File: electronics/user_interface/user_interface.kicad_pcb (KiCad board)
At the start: 2 copper layers, 100 x 100 mm, 44 parts, among them J1 Conn_01x06, J2 Conn_02x05_Odd_Even, U1 PCF8574, U2 PCF8574

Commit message: added ESD protection
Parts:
- added D5: 5V, SquantorDiodes:SOD-523, F.Cu at (114.0, 111.0)
- added D6: 5V, SquantorDiodes:SOD-523, F.Cu at (114.0, 131.0)
- added D7: 5V, SquantorDiodes:SOD-523, F.Cu at (158.0, 121.0)
- added D8: 5V, SquantorDiodes:SOD-523, F.Cu at (158.0, 141.0)
- moved R13 0.15 mm to (114.0, 133.0)
- moved R16 0.15 mm to (114.0, 135.0)
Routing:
- net Net-(D1-Pad2): track 10.3 -> 12.4 mm
- net /VSS: track 13.6 -> 14.4 mm, vias 0 -> 1
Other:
- rule pad_to_mask_clearance: 0.2 -> 0.1
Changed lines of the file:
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@@
     (thickness 1.6)
     (drawings 6)
-    (tracks 42)
+    (tracks 47)
     (zones 0)
-    (modules 44)
+    (modules 48)
     (nets 37)
   )
@@
     (pad_size 1.524 1.524)
     (pad_drill 0.762)
-    (pad_to_mask_clearance 0.2)
+    (pad_to_mask_clearance 0.1)
     (aux_axis_origin 0 0)
     (visible_elements FFFFFF7F)
@@
     (add_net "Net-(U2-Pad9)")
   )
+  (module SquantorDiodes:SOD-523 (layer F.Cu)
+    (at 158 141)
+    (fp_text reference D8 (at 0 -1.3) (layer F.SilkS)
+      (effects (font (size 1 1) (thickness 0.15)))
+    )
+    (fp_text value 5V (at 0 1.4) (layer F.Fab)
+      (effects (font (size 1 1) (thickness 0.15)))
+    )
+    (fp_line (start -1.1 -0.6) (end 1.1 -0.6) (layer F.CrtYd) (width 0.05))
+    (fp_line (start 1.1 -0.6) (end 1.1 0.6) (layer F.CrtYd) (width 0.05))
+    (fp_line (start 1.1 0.6) (end -1.1 0.6) (layer F.CrtYd) (width 0.05))
+    (fp_line (start -1.1 0.6) (end -1.1 -0.6) (layer F.CrtYd) (width 0.05))
+    (fp_line (start -0.3 -0.4) (end 0.3 -0.4) (layer F.SilkS) (width 0.15))
+    (fp_line (start 0.3 0.4) (end -0.3 0.4) (layer F.SilkS) (width 0.15))
+    (fp_line (start -0.3 -0.4) (end -0.3 0.4) (layer F.SilkS) (width 0.15))
+    (pad 2 smd rect (at 0.7 0) (size 0.5 0.6) (layers F.Cu F.Paste F.Mask)
+      (net 1 /VSS))
+    (pad 1 smd rect (at -0.7 0) (size 0.5 0.6) (layers F.Cu F.Paste F.Mask)
+      (net 36 "Net-(D4-Pad2)"))
+  )
+  (module SquantorDiodes:SOD-523 (layer F.Cu)
+    (at 158 121)
+    (fp_text reference D7 (at 0 -1.3) (layer F.SilkS)
+      (effects (font (size 1 1) (thickness 0.15)))
+    )
+    (fp_text value 5V (at 0 1.4) (layer F.Fab)
+      (effects (font (size 1 1) (thickness 0.15)))
+    )
+    (fp_line (start -1.1 -0.6) (end 1.1 -0.6) (layer F.CrtYd) (width 0.05))
+    (fp_line (start 1.1 -0.6) (end 1.1 0.6) (layer F.CrtYd) (width 0.05))
+    (fp_line (start 1.1 0.6) (end -1.1 0.6) (layer F.CrtYd) (width 0.05))
+    (fp_line (start -1.1 0.6) (end -1.1 -0.6) (layer F.CrtYd) (width 0.05))
+    (fp_line (start -0.3 -0.4) (end 0.3 -0.4) (layer F.SilkS) (width 0.15))
+    (fp_line (start 0.3 0.4) (end -0.3 0.4) (layer F.SilkS) (width 0.15))
+    (fp_line (start -0.3 -0.4) (end -0.3 0.4) (layer F.SilkS) (width 0.15))
+    (pad 2 smd rect (at 0.7 0) (size 0.5 0.6) (layers F.Cu F.Paste F.Mask)
+      (net 1 /VSS))
+    (pad 1 smd rect (at -0.7 0) (size 0.5 0.6) (layers F.Cu F.Paste F.Mask)
+      (net 35 "Net-(D3-Pad2)"))
+  )
+  (module SquantorDiodes:SOD-523 (layer F.Cu)
+    (at 114 131 180)
+    (fp_text reference D6 (at 2.4 0) (layer F.SilkS)
+      (effects (font (size 1 1) (thickness 0.15)))
+    )
+    (fp_text value 5V (at 0 1.3) (layer F.SilkS)
+      (effects (font (size 1 1) (thickness 0.15)))
+    )
+    (fp_line (start -1.1 -0.6) (end 1.1 -0.6) (layer F.CrtYd) (width 0.05))
+    (fp_line (start 1.1 -0.6) (end 1.1 0.6) (layer F.CrtYd) (width 0.05))
+    (fp_line (start 1.1 0.6) (end -1.1 0.6) (layer F.CrtYd) (width 0.05))
+    (fp_line (start -1.1 0.6) (end -1.1 -0.6) (layer F.CrtYd) (width 0.05))
+    (fp_line (start -0.3 -0.4) (end 0.3 -0.4) (layer F.SilkS) (width 0.15))
+    (fp_line (start 0.3 0.4) (end -0.3 0.4) (layer F.SilkS) (width 0.15))
+    (fp_line (start -0.3 -0.4) (end -0.3 0.4) (layer F.SilkS) (width 0.15))
+    (pad 2 smd rect (at 0.7 0 180) (size 0.5 0.6) (layers F.Cu F.Paste F.Mask)
+      (net 1 /VSS))
+    (pad 1 smd rect (at -0.7 0 180) (size 0.5 0.6) (layers F.Cu F.Paste F.Mask)
+      (net 34 "Net-(D2-Pad2)"))
+  )
+  (module SquantorDiodes:SOD-523 (layer F.Cu)
+    (at 114 111 180)
+    (fp_text reference D5 (at 2.6 0) (layer F.SilkS)
+      (effects (font (size 1 1) (thickness 0.15)))
+    )
+    (fp_text value 5V (at 0 1.3) (layer F.SilkS)
+      (effects (font (size 1 1) (thickness 0.15)))
+    )
+    (fp_line (start -1.1 -0.6) (end 1.1 -0.6) (layer F.CrtYd) (width 0.05))
+    (fp_line (start 1.1 -0.6) (end 1.1 0.6) (layer F.CrtYd) (width 0.05))
+    (fp_line (start 1.1 0.6) (end -1.1 0.6) (layer F.CrtYd) (width 0.05))
+    (fp_line (start -1.1 0.6) (end -1.1 -0.6) (layer F.CrtYd) (width 0.05))
+    (fp_line (start -0.3 -0.4) (end 0.3 -0.4) (layer F.SilkS) (width 0.15))
+    (fp_line (start 0.3 0.4) (end -0.3 0.4) (layer F.SilkS) (width 0.15))
+    (fp_line (start -0.3 -0.4) (end -0.3 0.4) (layer F.SilkS) (width 0.15))
+    (pad 2 smd rect (at 0.7 0 180) (size 0.5 0.6) (layers F.Cu F.Paste F.Mask)
+      (net 1 /VSS))
+    (pad 1 smd rect (at -0.7 0 180) (size 0.5 0.6) (layers F.Cu F.Paste F.Mask)
+      (net 30 "Net-(D1-Pad2)"))
+  )
   (module MX_Only:MXOnly-1U-NoLED (layer F.Cu)
     (at 146 136 270)
@@
   )
   (module SquantorRcl:R_0603_hand (layer F.Cu)
-    (at 113.85 135)
+    (at 114 135)
     (descr "Resistor SMD 0603, reflow soldering, Vishay (see dcrcw.pdf)")
     (tags "resistor 0603")
@@
   )
   (module SquantorRcl:R_0603_hand (layer F.Cu)
-    (at 113.85 133 180)
+    (at 114 133 180)
     (descr "Resistor SMD 0603, reflow soldering, Vishay (see dcrcw.pdf)")
     (tags "resistor 0603")
@@
   (segment (start 120.5 119) (end 121.31 119.81) (width 0.4) (layer F.Cu) (net 1))
   (segment (start 123.1 76.2) (end 127.65 76.2) (width 0.6) (layer F.Cu) (net 1))
+  (via (at 112.5 111) (size 0.6) (drill 0.3) (layers F.Cu B.Cu) (net 1))
+  (segment (start 113.3 111) (end 112.5 111) (width 0.4) (layer F.Cu) (net 1))
   (segment (start 129.15 78.2) (end 129.15 76.2) (width 0.4) (layer F.Cu) (net 2))
   (segment (start 129.15 76.2) (end 129.15 75.35) (width 0.4) (layer F.Cu) (net 2))
@@
   (segment (start 117.2 113) (end 114.85 113) (width 0.4) (layer F.Cu) (net 30))
   (segment (start 117.66 113.46) (end 117.2 113) (width 0.4) (layer F.Cu) (net 30))
+  (segment (start 114.85 113) (end 114.85 112.05) (width 0.4) (layer F.Cu) (net 30))
+  (segment (start 114.7 111.9) (end 114.7 111) (width 0.4) (layer F.Cu) (net 30))
+  (segment (start 114.85 112.05) (end 114.7 111.9) (width 0.4) (layer F.Cu) (net 30))
   (zone (net 1) (net_name /VSS) (layer B.Cu) (hatch edge 0.508)
     (connect_pads (clearance 0.4))

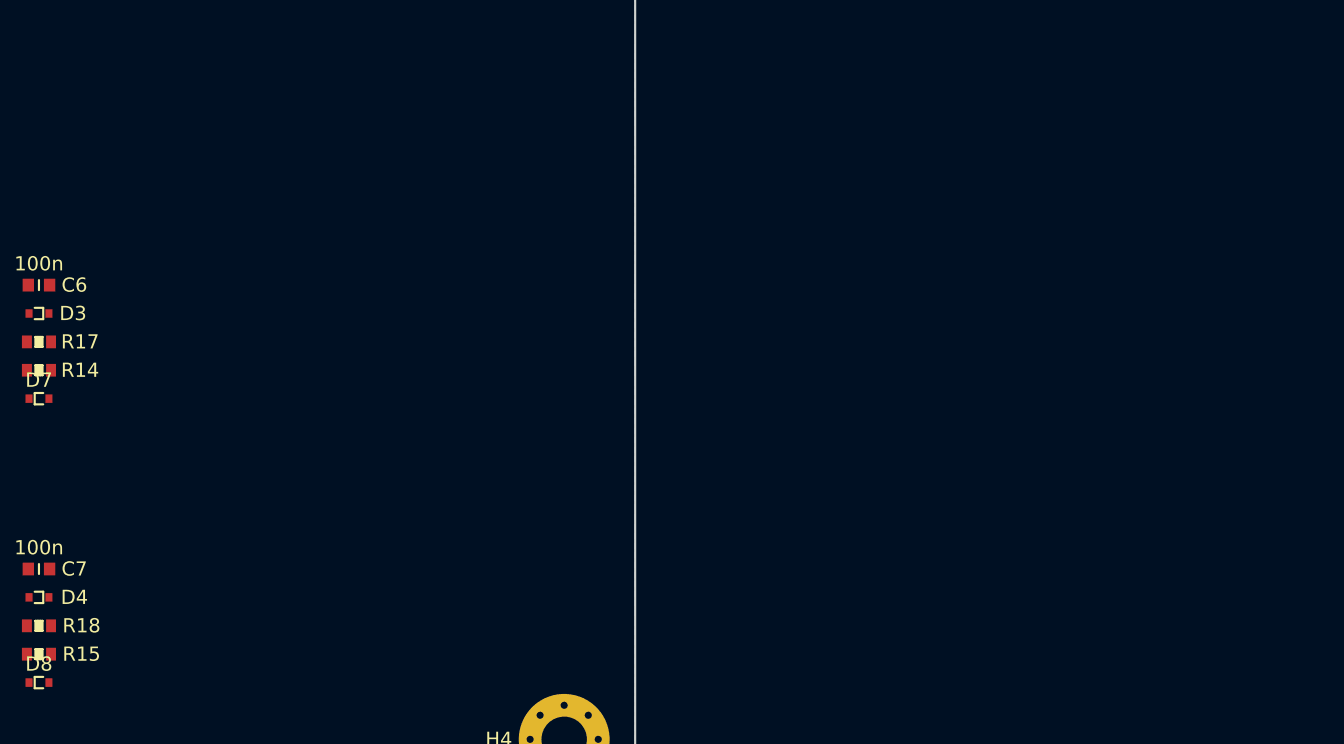
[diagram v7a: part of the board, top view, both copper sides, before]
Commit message: added rotary encoder knob to PCB
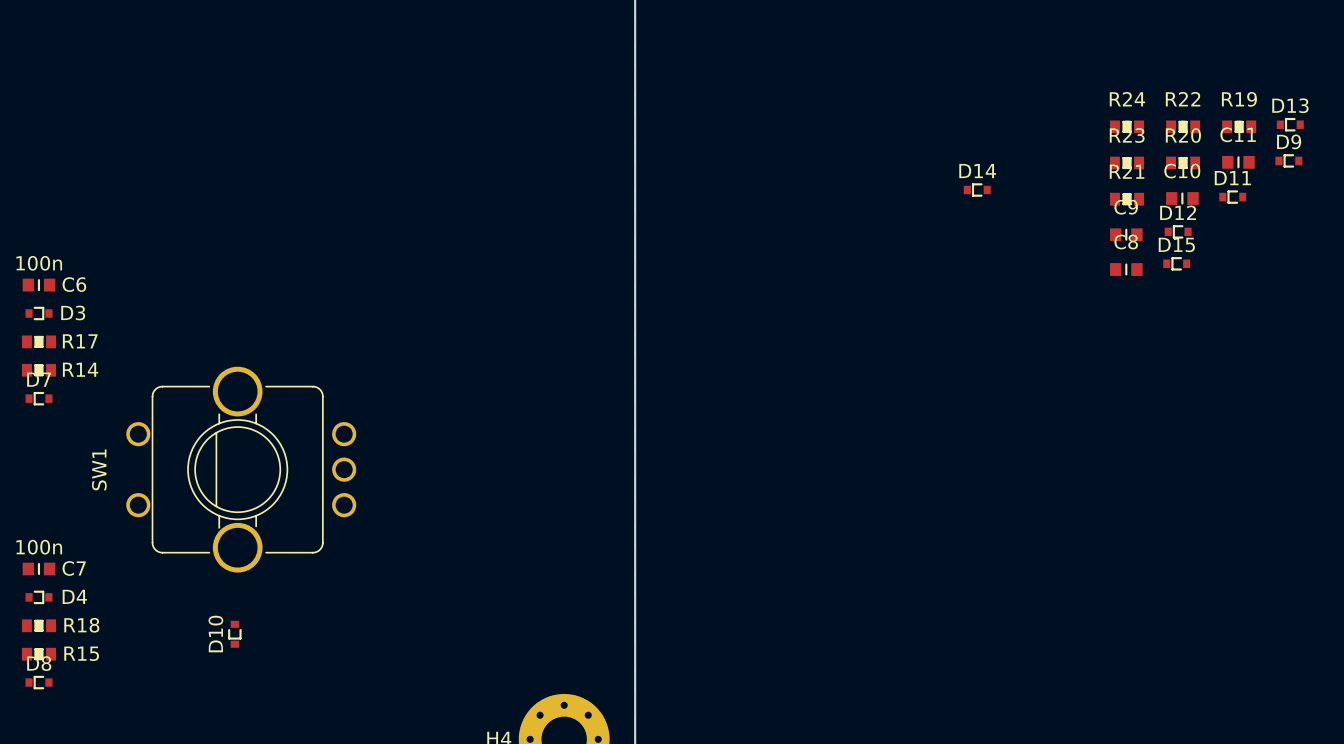
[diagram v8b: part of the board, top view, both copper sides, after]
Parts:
- added C10: 100n, SquantorRcl:C_0603, F.Cu at (238.6, 106.9)
- added C11: 100n, SquantorRcl:C_0603, F.Cu at (242.5, 104.3)
- added C8: 100n, SquantorRcl:C_0603, F.Cu at (234.6, 111.9)
- added C9: 100n, SquantorRcl:C_0603, F.Cu at (234.6, 109.5)
- added D10: 5V, SquantorDiodes:SOD-523, F.Cu at (171.8, 137.6)
- added D11: 5V, SquantorDiodes:SOD-523, F.Cu at (242.1, 106.8)
- added D12: RB521S-30, SquantorDiodes:SOD-523, F.Cu at (238.2, 109.2)
- added D13: RB521S-30, SquantorDiodes:SOD-523, F.Cu at (246.2, 101.7)
- added D14: RB521S-30, SquantorDiodes:SOD-523, F.Cu at (224.1, 106.3)
- added D15: 5V, SquantorDiodes:SOD-523, F.Cu at (238.2, 111.5)
- added D9: 5V, SquantorDiodes:SOD-523, F.Cu at (246.1, 104.2)
- added R19: TBD, SquantorRcl:R_0603_hand, F.Cu at (242.6, 101.8)
- added R20: TBD, SquantorRcl:R_0603_hand, F.Cu at (238.6, 104.4)
- added R21: TBD, SquantorRcl:R_0603_hand, F.Cu at (234.7, 107.0)
- added R22: TBD, SquantorRcl:R_0603_hand, F.Cu at (238.6, 101.8)
- added R23: TBD, SquantorRcl:R_0603_hand, F.Cu at (234.7, 104.4)
- added R24: TBD, SquantorRcl:R_0603_hand, F.Cu at (234.7, 101.8)
- added SW1: ALPS_EC11E18244A5, SquantorSwitches:ALPS_EC11E_style5, F.Cu at (172.0, 126.0)
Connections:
- U2 pad 10: Net-(U2-Pad10) -> /Rotary_B_filtered
- U2 pad 11: Net-(U2-Pad11) -> /Rotary_A_filtered
- U2 pad 12: Net-(U2-Pad12) -> /Rotary_push_filtered
